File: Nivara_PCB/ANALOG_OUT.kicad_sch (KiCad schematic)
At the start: 0 parts

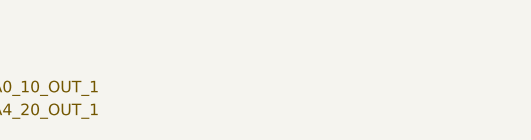
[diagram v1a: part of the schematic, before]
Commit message: Añadido de funciones NPN/PNP
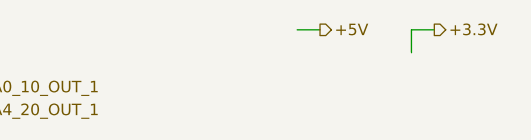
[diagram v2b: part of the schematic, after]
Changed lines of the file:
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@@
 	(generator_version "9.0")
 	(paper "A4")
+	(wire
+		(pts
+			(xy 81.28 58.42) (xy 83.82 58.42)
+		)
+		(stroke
+			(width 0)
+			(type default)
+		)
+	)
+	(wire
+		(pts
+			(xy 96.52 58.42) (xy 93.98 58.42)
+		)
+		(stroke
+			(width 0)
+			(type default)
+		)
+	)
+	(wire
+		(pts
+			(xy 93.98 58.42) (xy 93.98 60.96)
+		)
+		(stroke
+			(width 0)
+			(type default)
+		)
+	)
 	(hierarchical_label "A0_10_OUT_1"
 		(shape output)
@@
 		(effects
 			(font
+				(size 1.27 1.27)
+			)
+			(justify left)
+		)
+	)
+	(hierarchical_label "+5V"
+		(shape output)
+		(at 83.82 58.42 0)
+		(effects
+			(font
+				(size 1.27 1.27)
+			)
+			(justify left)
+		)
+	)
+	(hierarchical_label "+3.3V"
+		(shape output)
+		(at 96.52 58.42 0)
+		(effects
+			(font

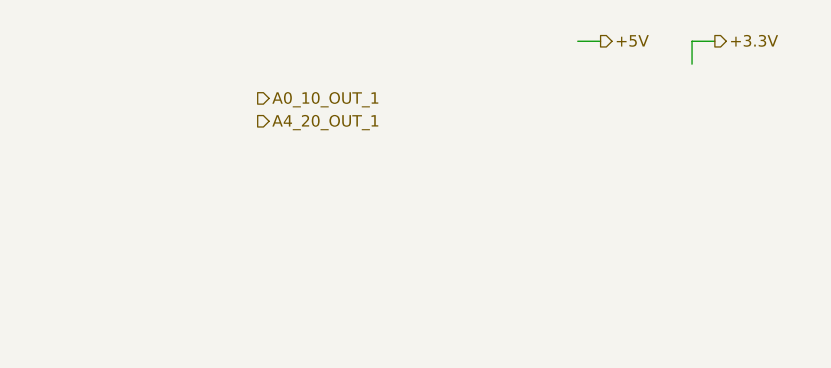
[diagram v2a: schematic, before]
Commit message: Cambios en el esquema de NPN y PNP
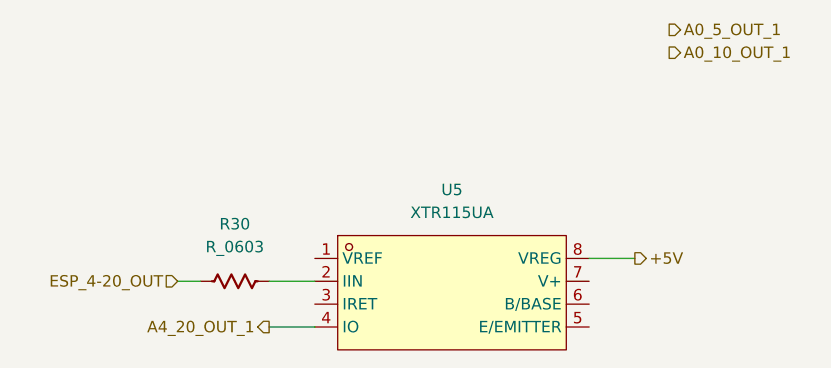
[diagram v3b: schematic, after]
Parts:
- added R30: R_0603, PCM_Resistor_SMD_AKL:R_0603_1608Metric, symbol PCM_Resistor_US_AKL:R_0603
- added U5: XTR115UA, Fuse_Holder:SOIC-8_L4.9-W3.9-P1.27-LS6.0-BL, symbol Fuse_Holder:XTR115UA
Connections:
- net +5V: now also U5.8 (VREG)
- net A4_20_OUT_1: now also U5.4 (IO)
- new net: R30.2, U5.2 (IIN)
- new net ESP_4-20_OUT: R30.1
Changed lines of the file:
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@@
 	(wire
 		(pts
-			(xy 81.28 58.42) (xy 83.82 58.42)
-		)
-		(stroke
-			(width 0)
-			(type default)
-		)
-	)
-	(wire
-		(pts
-			(xy 96.52 58.42) (xy 93.98 58.42)
-		)
-		(stroke
-			(width 0)
-			(type default)
-		)
-	)
-	(wire
-		(pts
-			(xy 93.98 58.42) (xy 93.98 60.96)
+			(xy 82.55 82.55) (xy 87.63 82.55)
+		)
+		(stroke
+			(width 0)
+			(type default)
+		)
+	)
+	(wire
+		(pts
+			(xy 46.99 90.17) (xy 52.07 90.17)
+		)
+		(stroke
+			(width 0)
+			(type default)
+		)
+	)
+	(wire
+		(pts
+			(xy 46.99 85.09) (xy 52.07 85.09)
+		)
+		(stroke
+			(width 0)
+			(type default)
+		)
+	)
+	(wire
+		(pts
+			(xy 36.83 85.09) (xy 39.37 85.09)
 		)
 		(stroke
@@
 	(hierarchical_label "A0_10_OUT_1"
 		(shape output)
-		(at 45.72 64.77 0)
+		(at 91.44 59.69 0)
 		(effects
 			(font
@@
 		)
 	)
+	(hierarchical_label "A0_5_OUT_1"
+		(shape output)
+		(at 91.44 57.15 0)
+		(effects
+			(font
+				(size 1.27 1.27)
+			)
+			(justify left)
+		)
+	)
 	(hierarchical_label "+5V"
 		(shape output)
-		(at 83.82 58.42 0)
+		(at 87.63 82.55 0)
 		(effects
 			(font
@@
 		)
 	)
-	(hierarchical_label "+3.3V"
-		(shape output)
-		(at 96.52 58.42 0)
-		(effects
-			(font
-				(size 1.27 1.27)
-			)
-			(justify left)
-		)
-	)
 	(hierarchical_label "A4_20_OUT_1"
 		(shape output)
-		(at 45.72 67.31 0)
-		(effects
-			(font
-				(size 1.27 1.27)
-			)
-			(justify left)
-		)
-	)
+		(at 46.99 90.17 180)
+		(effects
+			(font
+				(size 1.27 1.27)
+			)
+			(justify right)
+		)
+	)
+	(hierarchical_label "ESP_4-20_OUT"
+		(shape input)
+		(at 36.83 85.09 180)
+		(effects
+			(font
+				(size 1.27 1.27)
+			)
+			(justify right)
+		)
+	)
+	(symbol
+		(lib_id "Fuse_Holder:XTR115UA")
+		(at 67.31 86.36 0)
+		(unit 1)
+		(exclude_from_sim no)
+		(in_bom yes)
+		(on_board yes)
+		(dnp no)
+		(fields_autoplaced yes)
+		(property "Reference" "U5"
+			(at 67.31 74.93 0)
+			(effects
+				(font
+					(size 1.27 1.27)
+				)
+			)
+		)
+		(property "Value" "XTR115UA"
+			(at 67.31 77.47 0)
+			(effects
+				(font
+					(size 1.27 1.27)
+				)
+			)
+		)
+		(property "Footprint" "Fuse_Holder:SOIC-8_L4.9-W3.9-P1.27-LS6.0-BL"
+			(at 67.31 97.79 0)
+			(effects
+				(font
+					(size 1.27 1.27)
+				)
+				(hide yes)
+			)
+		)
+		(property "Datasheet" "https://lcsc.com/product-detail/4-20MA_TI_XTR115UA_XTR115UA_C21283.html"
+			(at 67.31 100.33 0)
+			(effects
+				(font
+					(size 1.27 1.27)
+				)
+				(hide yes)
+			)
+		)
+		(property "Description" ""
+			(at 67.31 86.36 0)
+			(effects
+				(font
+					(size 1.27 1.27)
+				)
+				(hide yes)
+			)
+		)
+		(property "LCSC Part" "C21283"
+			(at 67.31 102.87 0)
+			(effects
+				(font
+					(size 1.27 1.27)
+				)
+				(hide yes)
+			)
+		)
+		(pin "2"
+		)
+		(pin "1"
+		)
+		(pin "7"
+		)
+		(pin "3"
+		)
+		(pin "8"
+		)
+		(pin "4"
+		)
+		(pin "6"
+		)
+		(pin "5"
+		)
+		(instances
+			(project ""
+				(path "/13184db0-a71d-4054-b13a-bbf46d2b100d/4e7fa7f2-8bf5-4f9c-874d-fa1b4fd76f92/941ecd47-882f-406e-b54e-d369029f60e5"
+					(reference "U5")
+					(unit 1)
+				)
+			)
+		)
+	)
+	(symbol
+		(lib_id "PCM_Resistor_US_AKL:R_0603")
+		(at 43.18 85.09 90)
+		(unit 1)
+		(exclude_from_sim no)
+		(in_bom yes)
+		(on_board yes)
+		(dnp no)
+		(fields_autoplaced yes)
+		(property "Reference" "R30"
+			(at 43.18 78.74 90)
+			(effects
+				(font
+					(size 1.27 1.27)
+				)
+			)
+		)
+		(property "Value" "R_0603"
+			(at 43.18 81.28 90)
+			(effects
+				(font
+					(size 1.27 1.27)
+				)
+			)
+		)
+		(property "Footprint" "PCM_Resistor_SMD_AKL:R_0603_1608Metric"
+			(at 54.61 85.09 0)
+			(effects
+				(font
+					(size 1.27 1.27)
+				)
+				(hide yes)
+			)
+		)
+		(property "Datasheet" "~"
+			(at 43.18 85.09 0)
+			(effects
+				(font
+					(size 1.27 1.27)
+				)
+				(hide yes)
+			)
+		)
+		(property "Description" "SMD 0603 Chip Resistor, US Symbol, Alternate KiCad Library"
+			(at 43.18 85.09 0)
+			(effects
+				(font
+					(size 1.27 1.27)
+				)
+				(hide yes)
+			)
+		)
+		(pin "1"
+		)
+		(pin "2"
+		)
+		(instances
+			(project ""
+				(path "/13184db0-a71d-4054-b13a-bbf46d2b100d/4e7fa7f2-8bf5-4f9c-874d-fa1b4fd76f92/941ecd47-882f-406e-b54e-d369029f60e5"
+					(reference "R30")
+					(unit 1)
+				)
+			)
+		)
+	)

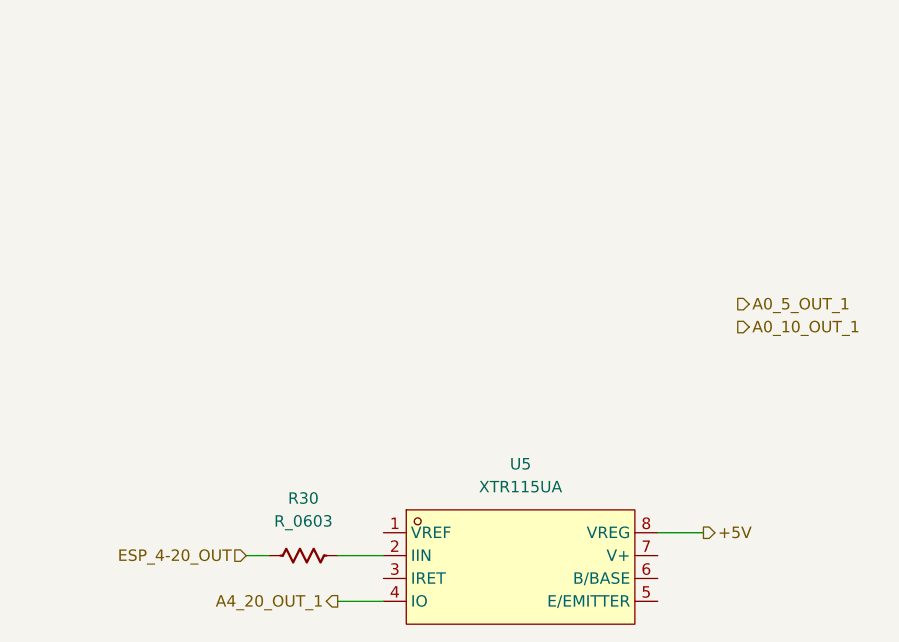
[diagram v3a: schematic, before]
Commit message: Cambios en las mediciones análogas.
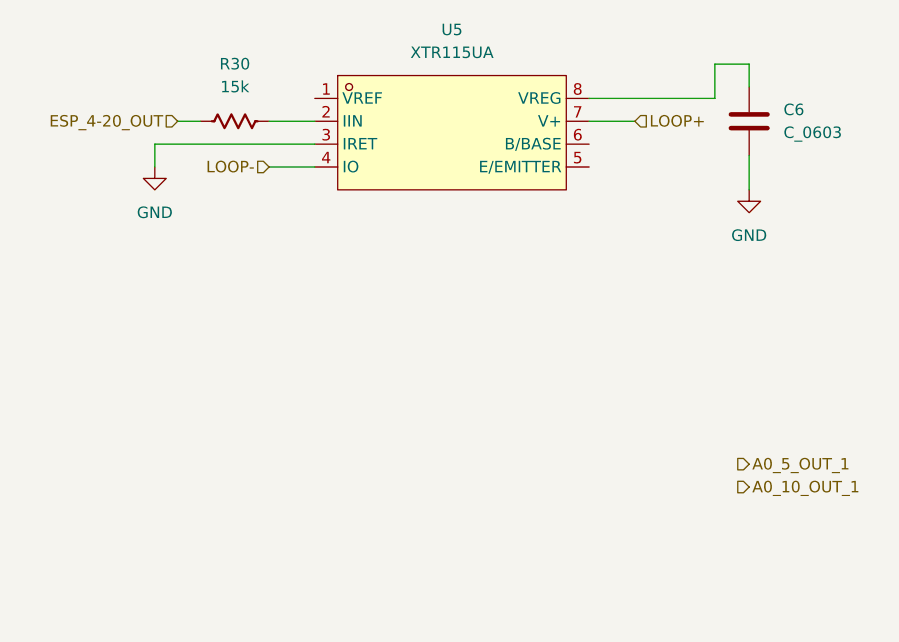
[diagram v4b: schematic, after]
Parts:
- added C6: C_0603, PCM_Capacitor_SMD_AKL:C_0603_1608Metric, symbol PCM_Capacitor_US_AKL:C_0603
- R30: value R_0603 -> 15k
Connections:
- net GND: now reaches U5.3 (IRET)
- net GND: now also C6.2
- net LOOP+: now reaches U5.7 (V+)
- net +5V: no longer names the net of U5.8 (VREG)
- net +5V: now also C6.1
- net A4_20_OUT_1 renamed LOOP-
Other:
- moved on the sheet: R30, U5

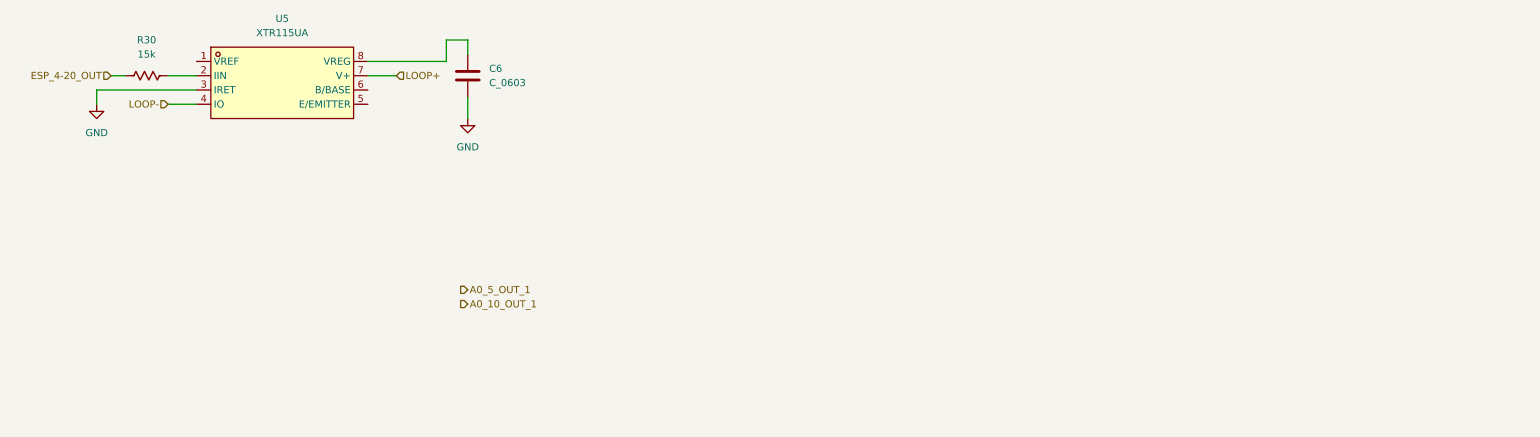
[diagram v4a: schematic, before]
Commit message: Cambios en las salidas analogicas, ya que el ESP32 S3 no tiene DAC
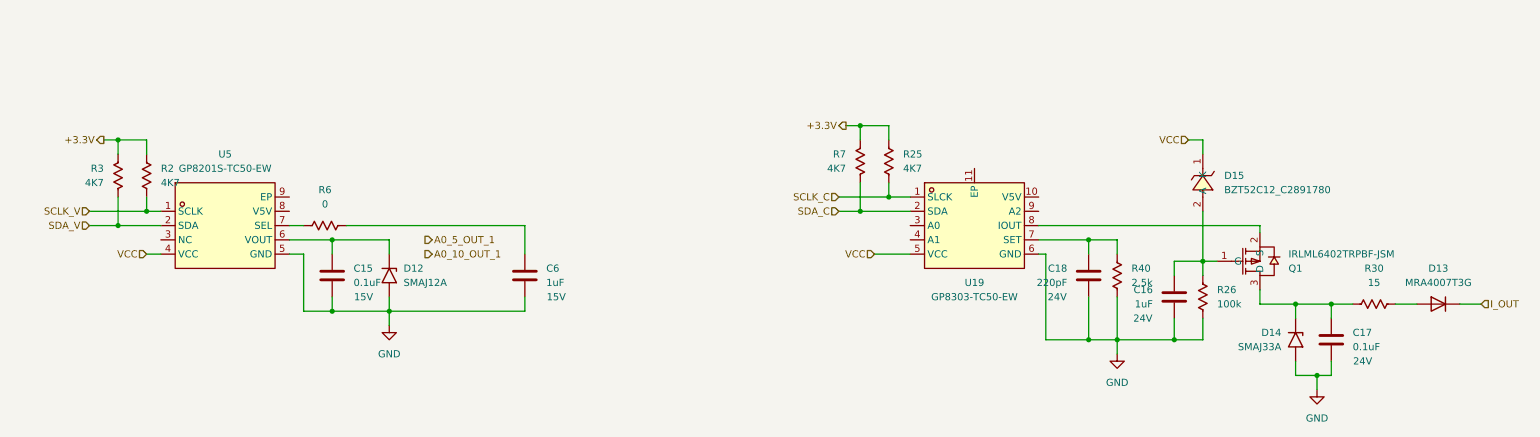
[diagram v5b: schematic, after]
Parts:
- removed R30: 15k, PCM_Resistor_SMD_AKL:R_0603_1608Metric, symbol PCM_Resistor_US_AKL:R_0603
- removed U5: XTR115UA, Fuse_Holder:SOIC-8_L4.9-W3.9-P1.27-LS6.0-BL, symbol Fuse_Holder:XTR115UA
- added C15, C17: 0.1uF, PCM_Capacitor_SMD_AKL:C_0603_1608Metric, symbol PCM_Capacitor_US_AKL:C_0603
- added C16: 1uF, PCM_Capacitor_SMD_AKL:C_0603_1608Metric, symbol PCM_Capacitor_US_AKL:C_0603
- added C18: 220pF, PCM_Capacitor_SMD_AKL:C_0603_1608Metric, symbol PCM_Capacitor_US_AKL:C_0603
- added D12: SMAJ12A, Diode_SMD:D_SMA, symbol Diode:SMAJ12A
- added D13: MRA4007T3G, Diode_SMD:D_SMA, symbol Diode:MRA4007T3G
- added D14: SMAJ33A, Diode_SMD:D_SMA, symbol Diode:SMAJ33A
- added D15: BZT52C12_C2891780, EasyEDA:SOD-123_L2.7-W1.6-LS3.7-RD-1, symbol EasyEDA:BZT52C12_C2891780
- added Q1: IRLML6402TRPBF-JSM, EasyEDA:SOT-23-3_L2.9-W1.3-P1.90-LS2.4-BR, symbol EasyEDA:IRLML6402TRPBF-JSM
- added R2, R25, R3, R7: 4K7, PCM_Resistor_SMD_AKL:R_0603_1608Metric, symbol PCM_Resistor_US_AKL:R_0603
- added R26: 100k, PCM_Resistor_SMD_AKL:R_0603_1608Metric, symbol PCM_Resistor_US_AKL:R_0603
- added R30: 15, PCM_Resistor_SMD_AKL:R_0805_2012Metric, symbol PCM_Resistor_US_AKL:R_0805
- added R40: 2.5k, PCM_Resistor_SMD_AKL:R_0603_1608Metric, symbol PCM_Resistor_US_AKL:R_0603
- added R6: 0, PCM_Resistor_SMD_AKL:R_0603_1608Metric, symbol PCM_Resistor_US_AKL:R_0603
- added U19: GP8303-TC50-EW, EasyEDA:ESOP-10_L4.9-W3.9-P1.00-LS6.1-BL-EP, symbol EasyEDA:GP8303-TC50-EW
- added U5: GP8201S-TC50-EW, EasyEDA:ESOP-8_L4.9-W3.9-P1.27-LS6.0-BL-EP, symbol EasyEDA:GP8201S-TC50-EW
- C6: value C_0603 -> 1uF; Vol (none) -> 15V
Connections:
- net GND: now also C15.2, C16.2, C17.2, C18.2, D12.2 (A2), D14.2 (A2), R26.2, R40.2, U19.6 (GND), U5.5 (GND)
- net at C6.1: now also R6.2
- new net: C18.1, R40.1, U19.7 (SET)
- new net: C15.1, D12.1 (A1), U5.6 (VOUT)
- new net: R6.1, U5.7 (SEL)
- new net: C16.1, D15.2 (A), Q1.1 (G), R26.1
- new net: Q1.2 (S), U19.8 (IOUT)
- new net: C17.1, D14.1 (A1), Q1.3 (D), R30.1
- new net: D13.2 (A), R30.2
- new net +3.3V: R2.1, R25.1, R3.1, R7.1
- new net I_OUT: D13.1 (K)
- new net SCLK_C: R25.2, U19.1 (SLCK)
- new net SCLK_V: R2.2, U5.1 (SCLK)
- new net SDA_C: R7.2, U19.2 (SDA)
- new net SDA_V: R3.2, U5.2 (SDA)
- new net VCC: D15.1 (K), U19.5 (VCC), U5.4 (VCC)
